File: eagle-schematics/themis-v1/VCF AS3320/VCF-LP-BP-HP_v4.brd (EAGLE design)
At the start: 83.8 x 64.4 mm, 38 parts

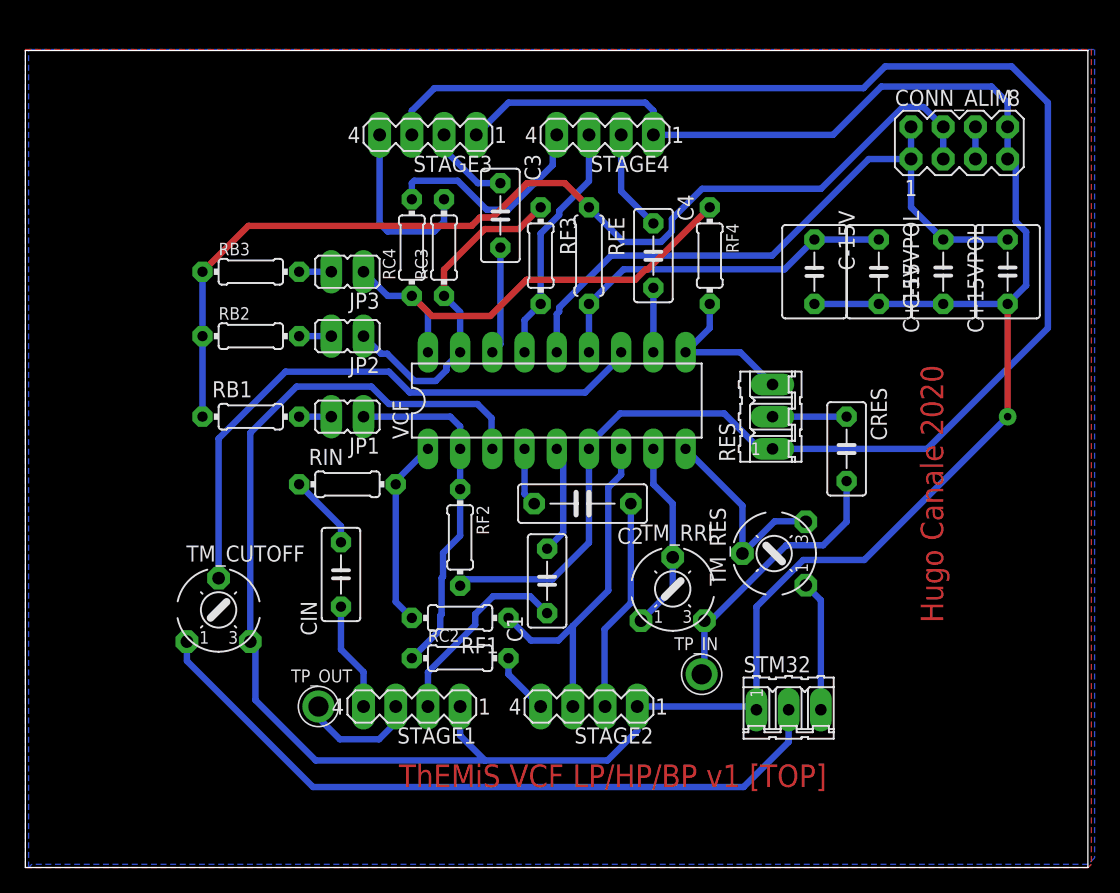
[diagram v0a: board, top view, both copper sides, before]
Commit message: Added new schematic for HP-LP-BP filter
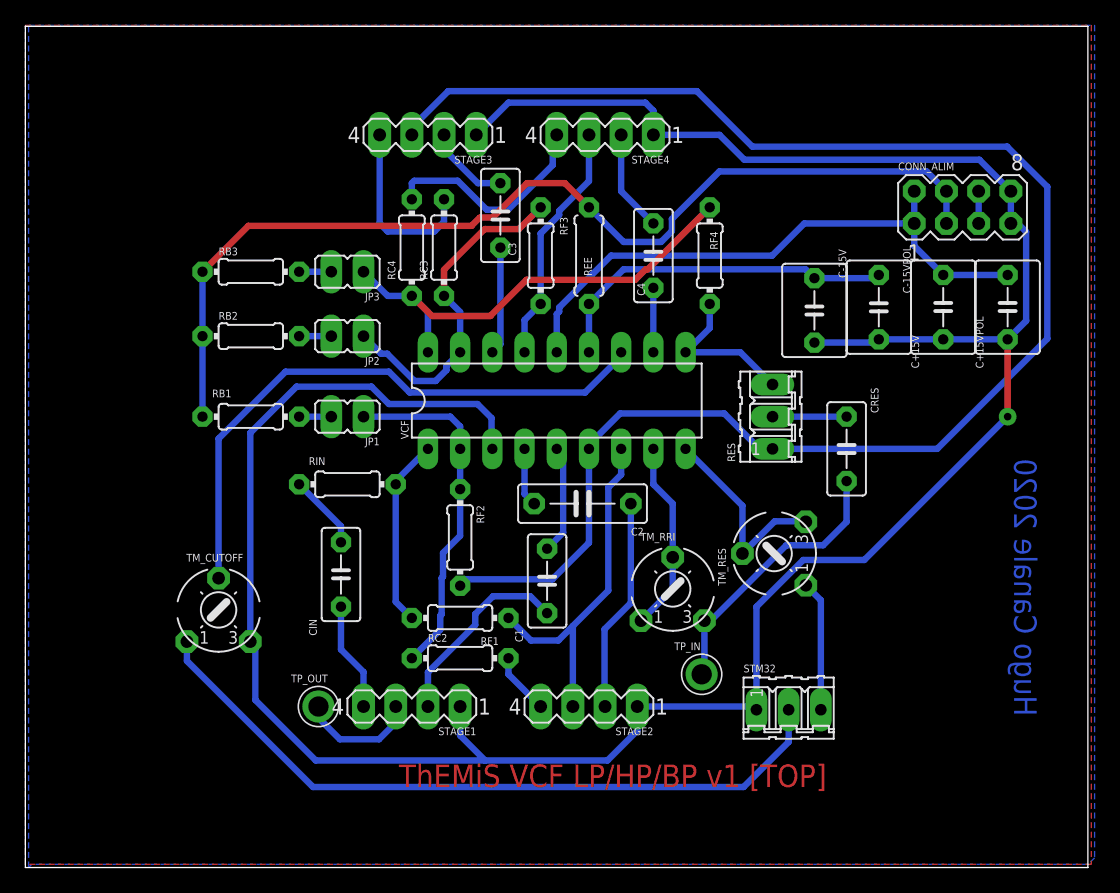
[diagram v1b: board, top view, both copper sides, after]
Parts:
- moved CONN_ALIM 5.09 mm to (73.9, 52.1)
- moved C-15V 3.05 mm to (62.2, 43.9)
- moved C+15V 2.79 mm to (72.4, 44.2)
- moved C+15VPOL 2.79 mm to (77.5, 44.2)
- moved C-15VPOL 2.79 mm to (67.3, 44.2)
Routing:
- net AGND: track 217.8 -> 210.7 mm
- net OUT2: track 134.1 -> 128.2 mm
- net +15V: track 51.2 -> 47.0 mm
- net -15V: track 82.8 -> 81.0 mm
- net VM3320: track 28.8 -> 28.2 mm
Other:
- board size 83.8 x 64.4 mm -> 83.8 x 66.3 mm
